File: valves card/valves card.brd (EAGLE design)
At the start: 100 x 80 mm, 72 parts, among them J1 TBP02R1-381-14BE, J2 09231486921, M2 SAM_D21_MINI_BREAKOUT, T1 IRLZ44NSTRLPBF, T10 IRLZ44NSTRLPBF, T11 IRLZ44NSTRLPBF, T12 IRLZ44NSTRLPBF, T2 IRLZ44NSTRLPBF, T3 IRLZ44NSTRLPBF, T4 IRLZ44NSTRLPBF, T5 IRLZ44NSTRLPBF, T6 IRLZ44NSTRLPBF, T7 IRLZ44NSTRLPBF, T8 IRLZ44NSTRLPBF, T9 IRLZ44NSTRLPBF, U1 LM2937IMP-12, U10 EL817(D)-ND, U11 EL817(D)-ND, U12 EL817(D)-ND, U13 EL817(D)-ND, U2 EL817(D)-ND, U3 EL817(D)-ND, U4 EL817(D)-ND, U5 EL817(D)-ND, U6 EL817(D)-ND, U7 EL817(D)-ND, U8 EL817(D)-ND, U9 EL817(D)-ND

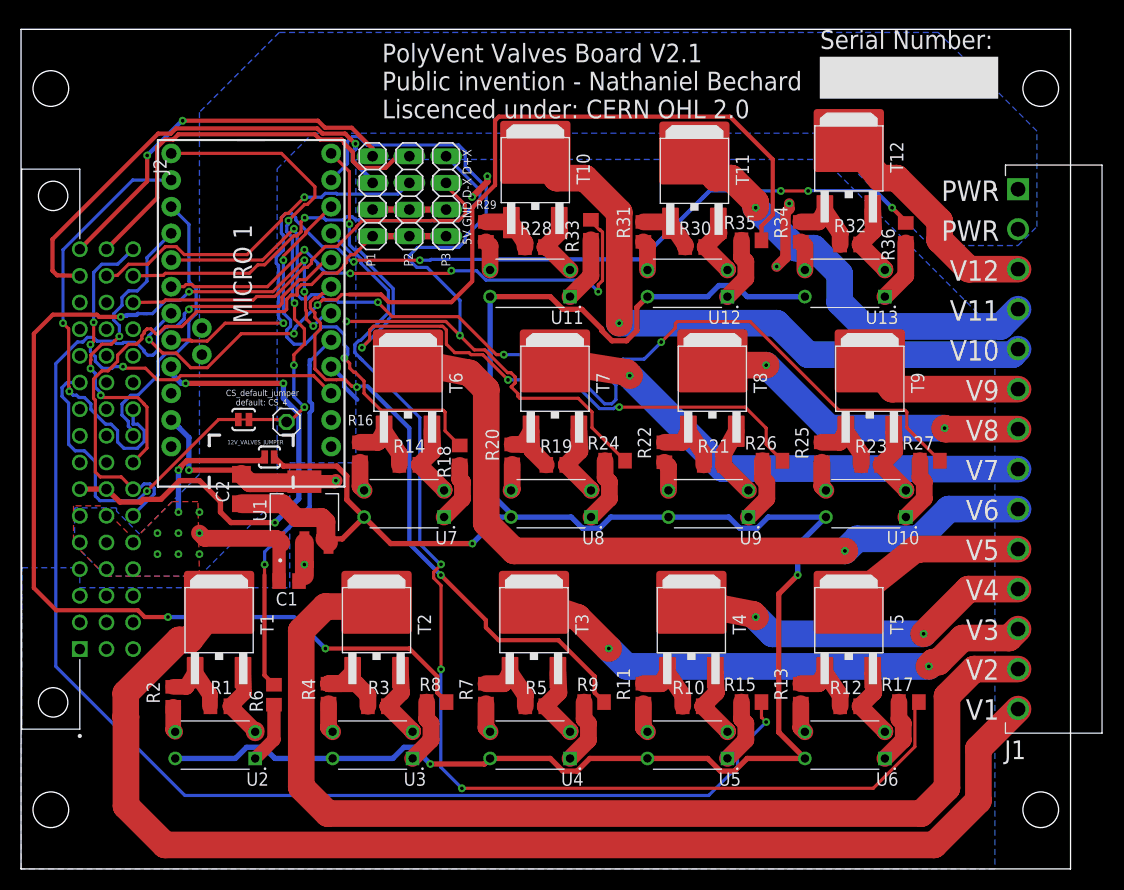
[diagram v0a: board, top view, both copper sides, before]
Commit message: updated libraries to generate better bom's
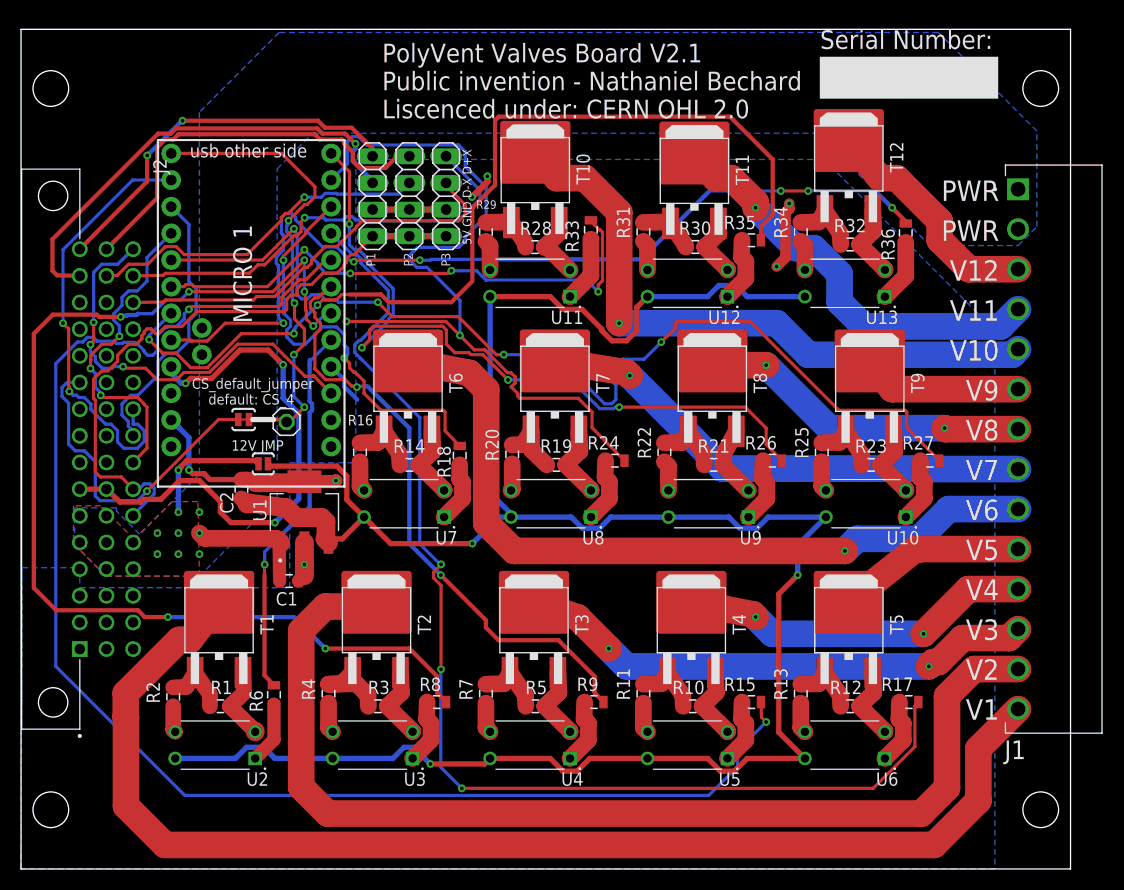
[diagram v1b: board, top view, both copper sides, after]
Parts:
- C1: value 0.1Uf -> 0.1Uf, 50V; device eagle-ltspice:C0805 -> SparkFun-Passives:0805
- C2: value 10Uf -> 10Uf, 50V; device eagle-ltspice:C1206 -> SparkFun-Passives:0805
- R1, R10, R11, R12, R13, R14, R15, R16, R17, R18, R19, R2, R20, R21, R22, R23, R24, R25, R26, R27, R28, R29, R3, R30, R31, R32, R33, R34, R35, R36, R4, R5, R6, R7, R8, R9: device eagle-ltspice:R0805 -> SparkFun-Passives:0805
- U10, U11, U12, U13, U2, U3, U4, U5, U6, U7, U8, U9: device EL817C:DIP762W25P254L650H453Q4B -> EL817(D):DIP4
- moved 12V_VALVES_JUMPER 0.88 mm to (23.1, 38.6)
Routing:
- net 3.3V: track 48.7 -> 52.4 mm
- net RESET: track 37.7 -> 40.3 mm
- net GND: track 128.7 -> 129.5 mm
- net 24V/12V: track 24.8 -> 24.2 mm
- net 12V: track 223.8 -> 224.3 mm
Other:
- board text added: "12V JMP"

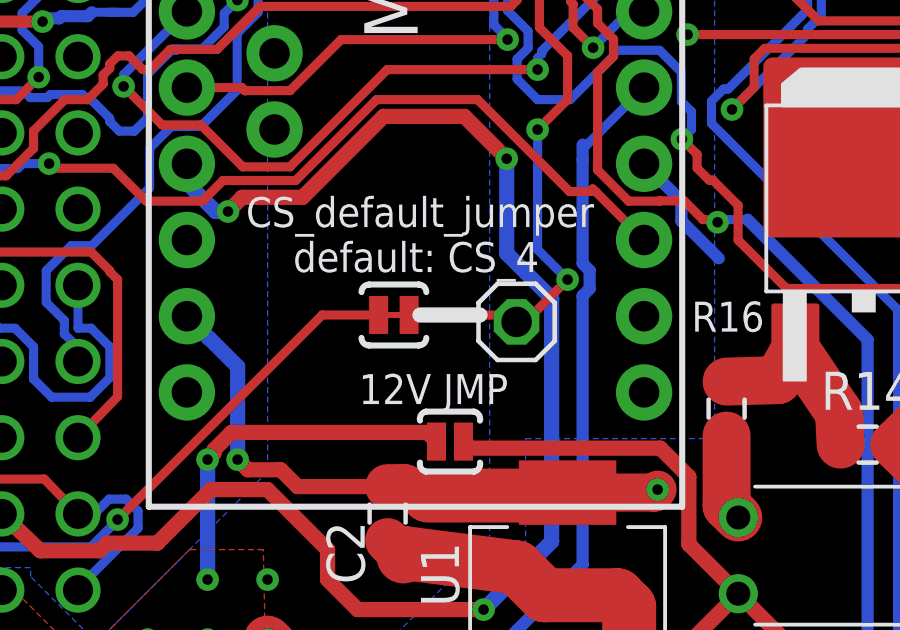
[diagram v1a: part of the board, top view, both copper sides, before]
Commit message: finished V2.2 control module update
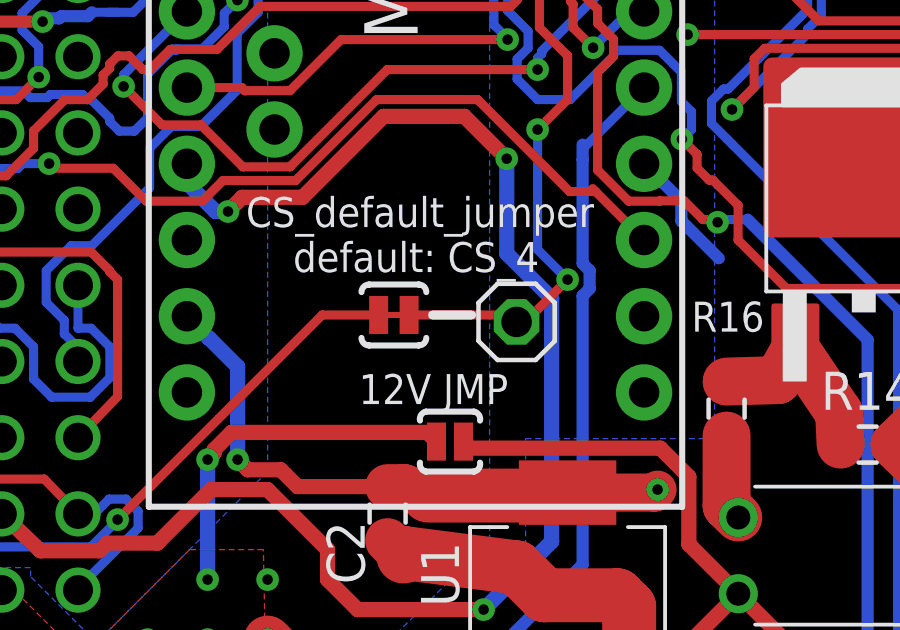
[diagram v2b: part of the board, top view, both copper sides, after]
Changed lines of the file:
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@@
 Public invention - Nathaniel Bechard
 Liscenced under: CERN OHL 2.0</text>
-<wire x1="22.08" y1="42.82" x2="24.08" y2="42.82" width="0.508" layer="21"/>
+<wire x1="22.5" y1="42.82" x2="23.8" y2="42.82" width="0.3048" layer="21"/>
 <text x="20.04" y="39.85" size="1" layer="25" distance="60">12V JMP</text>
 </plain>
